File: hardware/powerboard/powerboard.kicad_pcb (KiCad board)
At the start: 4 copper layers, 81.2 x 50.7 mm, 73 parts, among them J1 USB_B_Micro, J10 5V, J11 3V3, J2 Boot, J3 Keysboard Header, J4 Display, J5 Debug, J7 UART_0, J8 I2C_0, J9 I2C_1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

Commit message: Last Thicky Update
More thickening
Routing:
- net GND: track 93.7 -> 105.9 mm, vias 127 -> 143
- net SPI_RX_1: track 26.5 -> 21.7 mm
- net /QSPI_SS: track 30.3 -> 27.1 mm
- net /XIN: track 14.2 -> 14.8 mm
- net /XOUT: track 6.34 -> 6.89 mm
- net +5V: track 19.3 -> 18.8 mm

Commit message: 3.3V Header Fix
Both sides of the 3.3V header were on the same +3.3V net, this means that the copper fill on Layer 3 would have connected the header, not the jumper we plan to use. This would have likely broken one of our multimeters if we left it unchanged, and would make power measurements near impossible. The new power net on the output of the DCDC converter is VDD, which goes to one side of the 3.3V pin header, and the +3.3V net is on the other side.
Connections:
- C29 pad 1: +3.3V -> VDD
- C30 pad 1: +3.3V -> VDD
- C31 pad 1: +3.3V -> VDD
- C32 pad 1: +3.3V -> VDD
- C4 pad 1: +3.3V -> VDD
- J11 pad 1: +3.3V -> VDD
- L1 pad 2: +3.3V -> VDD
- U2 pad 5: +3.3V -> VDD
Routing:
- net VDD: track 0.00 -> 20.5 mm
- net +3.3V: track 92.6 -> 72.1 mm
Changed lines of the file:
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@@
   (net 64 "Net-(R13-Pad1)")
   (net 65 "Net-(R14-Pad1)")
+  (net 66 "VDD")
   (footprint "Button_Switch_THT:SW_PUSH_6mm" (layer "F.Cu")
     (at 119.0002 37.374)
@@
     (fp_line (start 1 0.625) (end -1 0.625) (layer "F.Fab") (width 0.1))
     (pad "1" smd roundrect (at -0.95 0) (size 1 1.45) (layers "F.Cu" "F.Paste" "F.Mask") (roundrect_rratio 0.25)
-      (net 2 "+3.3V") (pintype "passive"))
+      (net 66 "VDD") (pintype "passive"))
     (pad "2" smd roundrect (at 0.95 0) (size 1 1.45) (layers "F.Cu" "F.Paste" "F.Mask") (roundrect_rratio 0.25)
       (net 1 "GND") (pintype "passive"))
@@
     (fp_line (start -1 0.625) (end -1 -0.625) (layer "F.Fab") (width 0.1))
     (pad "1" smd roundrect (at -0.95 0) (size 1 1.45) (layers "F.Cu" "F.Paste" "F.Mask") (roundrect_rratio 0.25)
-      (net 2 "+3.3V") (pintype "passive"))
+      (net 66 "VDD") (pintype "passive"))
     (pad "2" smd roundrect (at 0.95 0) (size 1 1.45) (layers "F.Cu" "F.Paste" "F.Mask") (roundrect_rratio 0.25)
       (net 1 "GND") (pintype "passive"))
@@
       (net 17 "Net-(L1-Pad1)") (pinfunction "Lx") (pintype "output"))
     (pad "5" smd roundrect (at 1.1375 -0.95) (size 1.325 0.6) (layers "F.Cu" "F.Paste" "F.Mask") (roundrect_rratio 0.25)
-      (net 2 "+3.3V") (pinfunction "Vout") (pintype "power_out"))
+      (net 66 "VDD") (pinfunction "Vout") (pintype "power_out"))
     (model "${KICAD6_3DMODEL_DIR}/Package_TO_SOT_SMD.3dshapes/TSOT-23-5.wrl"
       (offset (xyz 0 0 0))
@@
     (fp_line (start 1 0.625) (end -1 0.625) (layer "F.Fab") (width 0.1))
     (pad "1" smd roundrect (at -0.95 0) (size 1 1.45) (layers "F.Cu" "F.Paste" "F.Mask") (roundrect_rratio 0.25)
-      (net 2 "+3.3V") (pintype "passive"))
+      (net 66 "VDD") (pintype "passive"))
     (pad "2" smd roundrect (at 0.95 0) (size 1 1.45) (layers "F.Cu" "F.Paste" "F.Mask") (roundrect_rratio 0.25)
       (net 1 "GND") (pintype "passive"))
@@
     (fp_line (start 1 0.625) (end -1 0.625) (layer "F.Fab") (width 0.1))
     (pad "1" smd roundrect (at -0.95 0) (size 1 1.45) (layers "F.Cu" "F.Paste" "F.Mask") (roundrect_rratio 0.25)
-      (net 2 "+3.3V") (pintype "passive"))
+      (net 66 "VDD") (pintype "passive"))
     (pad "2" smd roundrect (at 0.95 0) (size 1 1.45) (layers "F.Cu" "F.Paste" "F.Mask") (roundrect_rratio 0.25)
       (net 1 "GND") (pintype "passive"))
@@
     (fp_line (start -1.27 3.81) (end -1.27 -0.635) (layer "F.Fab") (width 0.1))
     (pad "1" thru_hole rect (at 0 0 180) (size 1.7 1.7) (drill 1) (layers *.Cu *.Mask)
-      (net 2 "+3.3V") (pinfunction "Pin_1") (pintype "passive"))
+      (net 66 "VDD") (pinfunction "Pin_1") (pintype "passive"))
     (pad "2" thru_hole oval (at 0 2.54 180) (size 1.7 1.7) (drill 1) (layers *.Cu *.Mask)
       (net 2 "+3.3V") (pinfunction "Pin_2") (pintype "passive"))
@@
       (net 17 "Net-(L1-Pad1)") (pinfunction "1") (pintype "passive"))
     (pad "2" smd roundrect (at 2.1375 0 90) (size 1.125 3.4) (layers "F.Cu" "F.Paste" "F.Mask") (roundrect_rratio 0.2222222222)
-      (net 2 "+3.3V") (pinfunction "2") (pintype "passive"))
+      (net 66 "VDD") (pinfunction "2") (pintype "passive"))
     (model "${KICAD6_3DMODEL_DIR}/Inductor_SMD.3dshapes/L_1812_4532Metric.wrl"
       (offset (xyz 0 0 0))
@@
     (fp_line (start 1 -0.625) (end 1 0.625) (layer "F.Fab") (width 0.1))
     (pad "1" smd roundrect (at -0.95 0) (size 1 1.45) (layers "F.Cu" "F.Paste" "F.Mask") (roundrect_rratio 0.25)
-      (net 2 "+3.3V") (pintype "passive"))
+      (net 66 "VDD") (pintype "passive"))
     (pad "2" smd roundrect (at 0.95 0) (size 1 1.45) (layers "F.Cu" "F.Paste" "F.Mask") (roundrect_rratio 0.25)
       (net 1 "GND") (pintype "passive"))
@@
   (segment (start 113.9444 51.3466) (end 115.0752 50.2158) (width 0.29337) (layer "F.Cu") (net 2))
   (segment (start 76.006308 35.6236) (end 76.3144 35.6236) (width 0.2) (layer "F.Cu") (net 2))
-  (segment (start 89.6264 17.145) (end 89.6264 25.7923) (width 1) (layer "F.Cu") (net 2))
   (segment (start 75.9144 46.5644) (end 75.9144 45.9802) (width 0.29337) (layer "F.Cu") (net 2))
-  (segment (start 96.9264 26.6192) (end 96.9264 25.7098) (width 0.4) (layer "F.Cu") (net 2))
   (segment (start 73.2282 28.7274) (end 73.2028 28.7528) (width 0.2) (layer "F.Cu") (net 2))
-  (segment (start 90.8812 27.0471) (end 96.4985 27.0471) (width 0.6) (layer "F.Cu") (net 2))
   (segment (start 81.0514 37.1094) (end 80.8736 37.2872) (width 0.2) (layer "F.Cu") (net 2))
   (segment (start 78.2828 35.2806) (end 77.9144 35.649) (width 0.2) (layer "F.Cu") (net 2))
   (segment (start 80.391 40.5638) (end 80.2386 40.7162) (width 0.29337) (layer "F.Cu") (net 2))
   (segment (start 98.044 19.2024) (end 98.031 19.1894) (width 0.2) (layer "F.Cu") (net 2))
-  (segment (start 90.8545 27.0204) (end 90.8812 27.0471) (width 0.4) (layer "F.Cu") (net 2))
   (segment (start 70.017647 41.367178) (end 70.490825 40.894) (width 0.29337) (layer "F.Cu") (net 2))
   (segment (start 79.96845 37.24565) (end 79.1519 37.24565) (width 0.2) (layer "F.Cu") (net 2))
-  (segment (start 96.4985 27.0471) (end 96.9264 26.6192) (width 0.6) (layer "F.Cu") (net 2))
   (segment (start 75.8444 46.6344) (end 75.9144 46.5644) (width 0.2) (layer "F.Cu") (net 2))
   (segment (start 77.9144 35.649) (end 77.9144 36.40815) (width 0.2) (layer "F.Cu") (net 2))
@@
   (segment (start 70.6882 40.894) (end 70.73655 40.84565) (width 0.2) (layer "F.Cu") (net 2))
   (segment (start 80.8482 37.2618) (end 79.9846 37.2618) (width 0.29337) (layer "F.Cu") (net 2))
-  (segment (start 89.6264 25.7923) (end 90.8812 27.0471) (width 1) (layer "F.Cu") (net 2))
   (segment (start 78.5622 35.7886) (end 79.8068 35.7886) (width 0.29337) (layer "F.Cu") (net 2))
   (segment (start 80.2386 40.7162) (end 80.10915 40.84565) (width 0.2) (layer "F.Cu") (net 2))
-  (segment (start 87.93165 27.0204) (end 90.8545 27.0204) (width 0.6) (layer "F.Cu") (net 2))
   (segment (start 80.10915 40.84565) (end 79.1519 40.84565) (width 0.2) (layer "F.Cu") (net 2))
   (segment (start 113.6756 60.6298) (end 114.999 59.3064) (width 0.29337) (layer "F.Cu") (net 2))
@@
   (segment (start 110.3882 27.8384) (end 110.5806 27.646) (width 0.25) (layer "F.Cu") (net 65))
   (segment (start 108.3686 27.8384) (end 110.3882 27.8384) (width 0.29337) (layer "F.Cu") (net 65))
+  (segment (start 89.6264 17.145) (end 89.6264 25.7923) (width 1) (layer "F.Cu") (net 66))
+  (segment (start 96.9264 26.6192) (end 96.9264 25.7098) (width 0.4) (layer "F.Cu") (net 66))
+  (segment (start 90.8812 27.0471) (end 96.4985 27.0471) (width 0.6) (layer "F.Cu") (net 66))
+  (segment (start 90.8545 27.0204) (end 90.8812 27.0471) (width 0.4) (layer "F.Cu") (net 66))
+  (segment (start 96.4985 27.0471) (end 96.9264 26.6192) (width 0.6) (layer "F.Cu") (net 66))
+  (segment (start 89.6264 25.7923) (end 90.8812 27.0471) (width 1) (layer "F.Cu") (net 66))
+  (segment (start 87.93165 27.0204) (end 90.8545 27.0204) (width 0.6) (layer "F.Cu") (net 66))
   (zone (net 0) (net_name "") (layers "F.Cu" "In1.Cu" "In2.Cu" "B.Cu") (hatch edge 0.508)
     (connect_pads (clearance 0))

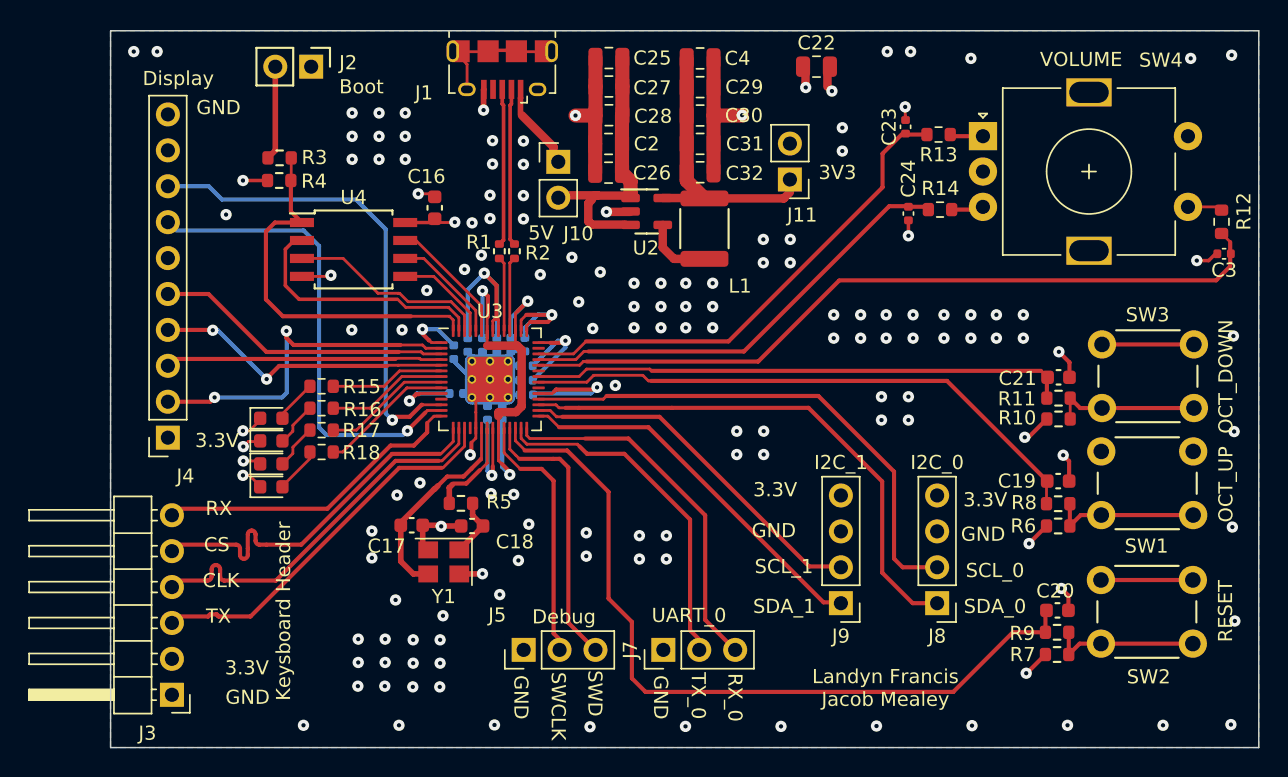
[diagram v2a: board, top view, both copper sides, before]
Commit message: More trace spacing
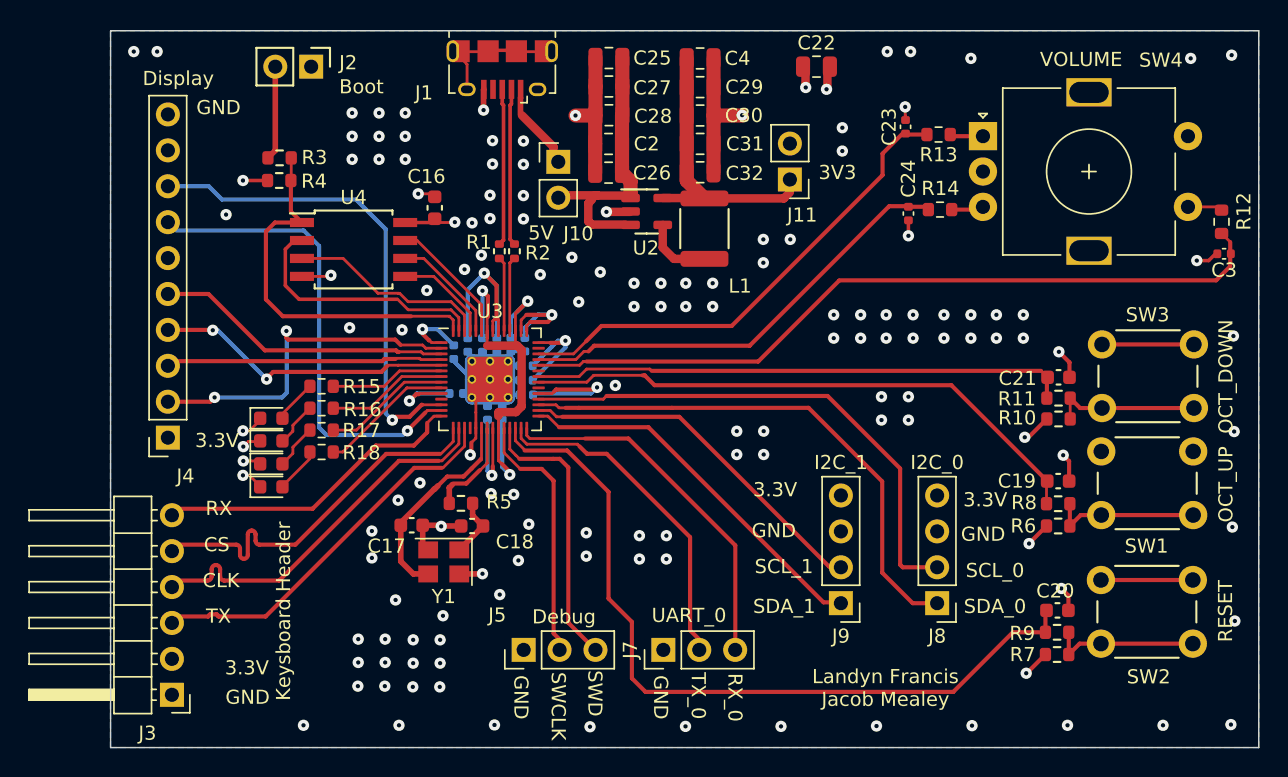
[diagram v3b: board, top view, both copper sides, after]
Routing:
- net UART_TX_0: track 23.8 -> 23.1 mm
- net A: track 35.3 -> 34.8 mm
- net GND: track 105.9 -> 105.7 mm, vias 143 -> 137
